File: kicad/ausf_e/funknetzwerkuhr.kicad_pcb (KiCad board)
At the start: 2 copper layers, 100 x 80 mm, 110 parts, among them J1 Jack-DC, J2 Conn_01x04_Male, J3 Conn_01x02_Male, J4 Conn_01x04_Male, Q1 IRF640, Q10 MMBTA42, Q11 MMBTA42, Q12 MMBTA42, Q13 MMBTA42, Q14 MMBTA42, Q15 MMBTA42, Q16 MMBTA42, Q17 MMBTA42, Q18 MMBTA42, Q19 MMBTA42, Q2 MMBTA42, Q20 MMBTA42, Q21 MMBTA42, Q22 MMBTA42, Q3 MMBTA92, Q4 MMBTA42, Q5 MMBTA92, Q6 MMBTA42, Q7 MMBTA92, Q8 MMBTA42, Q9 MMBTA92, T1 IN-12, T2 IN-12, T3 IN-12, T4 IN-12, U1 74HC595, U2 74HC595, U3 74HC595, U4 max1771, U5 NCP1117-33G, U6 ESP-12E

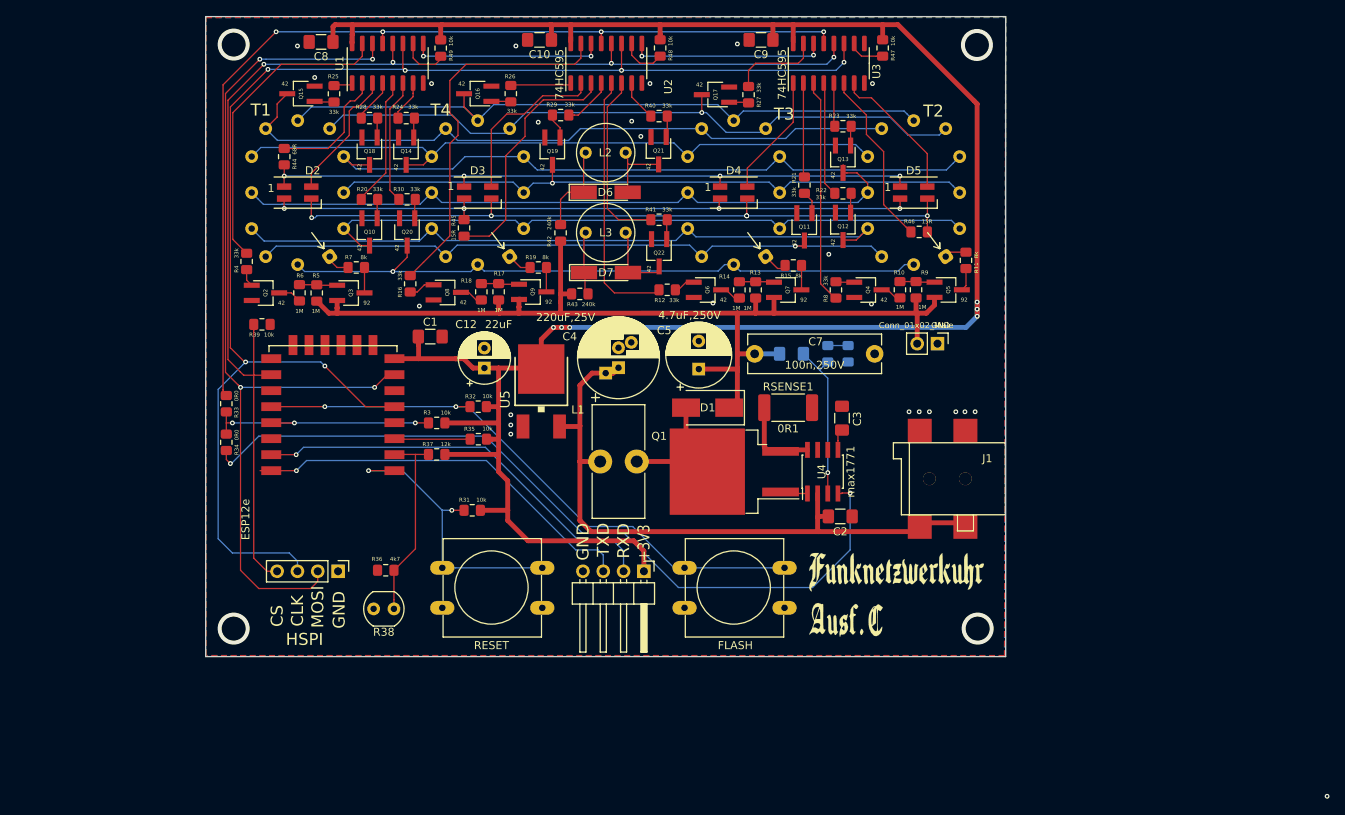
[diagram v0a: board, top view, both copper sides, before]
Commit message: Switched from NTPTime to ezTime
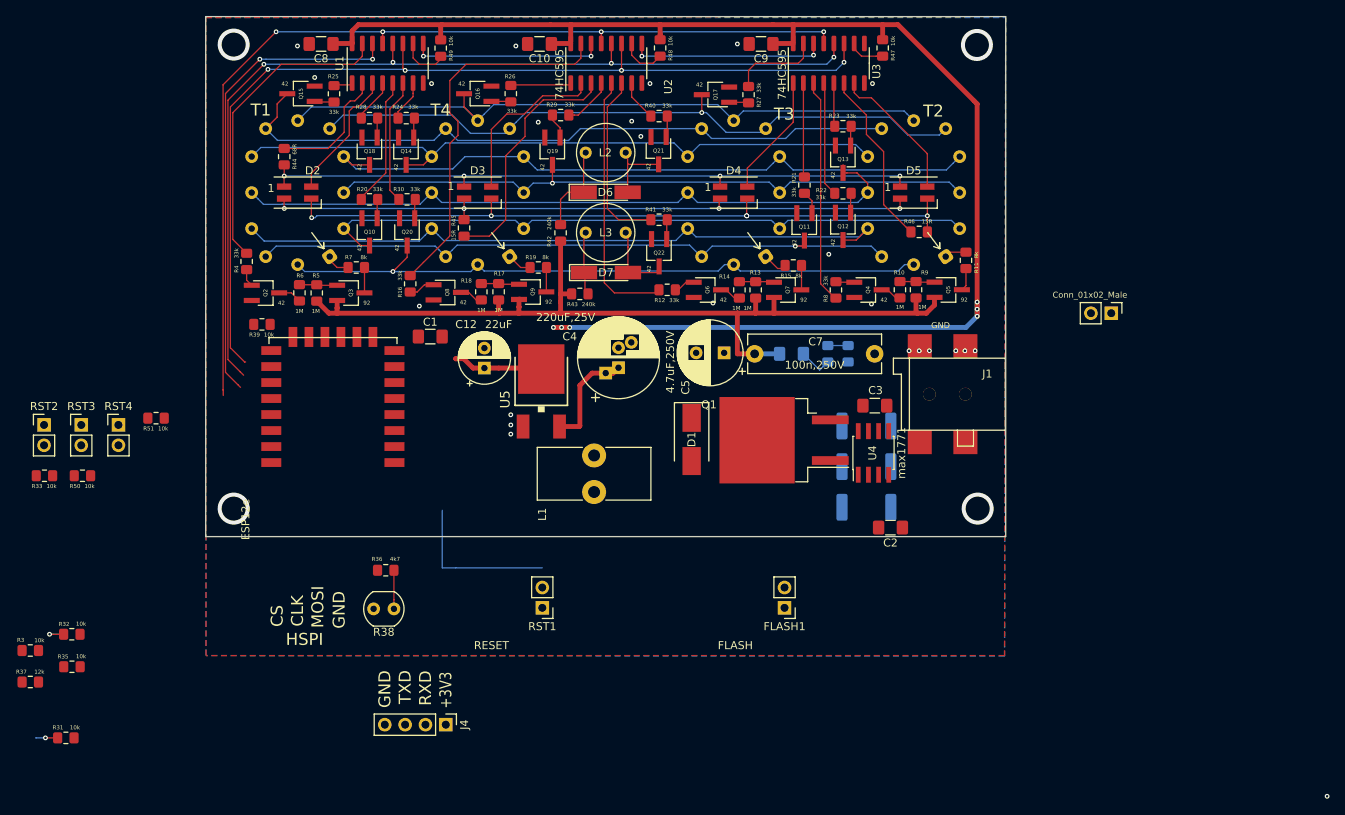
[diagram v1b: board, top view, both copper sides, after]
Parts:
- removed G***: LOGO, PartsStash:Funknetzwerkuhr_Ausf_C
- removed J2: Conn_01x04_Male, Connector_PinHeader_2.54mm:PinHeader_1x04_P2.54mm_Vertical
- removed R34: 0R0, PartsStash:R_0805_2012Metric_Pad1.15x1.40mm_HandSolder_Value
- added R50: 10k, PartsStash:R_0805_2012Metric_Pad1.15x1.40mm_HandSolder_Value, F.Cu at (34.6, 112.4)
- added R51: 10k, PartsStash:R_0805_2012Metric_Pad1.15x1.40mm_HandSolder_Value, F.Cu at (43.8, 105.2)
- added RSENSE2: 0R1, Resistor_SMD:R_2512_6332Metric_Pad1.40x3.35mm_HandSolder, B.Cu at (132.6, 106.2)
- added RSENSE3: 0R1, Resistor_SMD:R_2512_6332Metric_Pad1.40x3.35mm_HandSolder, B.Cu at (132.6, 116.3)
- added RST2: SW_DIP_x01, Connector_PinHeader_2.54mm:PinHeader_1x02_P2.54mm_Vertical, F.Cu at (29.8, 106.0)
- added RST3: SW_DIP_x01, Connector_PinHeader_2.54mm:PinHeader_1x02_P2.54mm_Vertical, F.Cu at (34.4, 106.0)
- added RST4: SW_DIP_x01, Connector_PinHeader_2.54mm:PinHeader_1x02_P2.54mm_Vertical, F.Cu at (39.1, 106.0)
- FLASH1, RST1: footprint Button_Switch_THT:SW_PUSH-12mm -> Connector_PinHeader_2.54mm:PinHeader_1x02_P2.54mm_Vertical
- J4: footprint Connector_PinHeader_2.54mm:PinHeader_1x04_P2.54mm_Horizontal -> Connector_PinHeader_2.54mm:PinHeader_1x04_P2.54mm_Vertical
- R33: value 0R0 -> 10k
- RSENSE1: footprint Resistor_SMD:R_2512_6332Metric_Pad1.52x3.35mm_HandSolder -> Resistor_SMD:R_2512_6332Metric_Pad1.40x3.35mm_HandSolder; moved to B.Cu
- moved R3 58.2 mm to (28.1, 134.2)
- moved R31 58.2 mm to (32.5, 145.2)
- moved R37 58.2 mm to (28.1, 138.2)
- moved R32 58.2 mm to (33.3, 132.2)
- moved R35 58.2 mm to (33.3, 136.3)
- moved J4 31.3 mm to (80.0, 143.5)
- moved R33 24.5 mm to (29.8, 112.4), turned to 0 degrees
- moved J3 22.0 mm to (163.2, 92.1)
- moved RSENSE1 12.2 mm to (132.6, 111.3)
- moved J1 10.6 mm to (145.0, 102.2)
- moved Q1 7.36 mm to (122.3, 108.0)
- moved U4 6.77 mm to (133.5, 109.5)
- moved C2 6.43 mm to (135.6, 118.9)
- moved D1 4.44 mm to (110.7, 107.9), turned to 270 degrees
- moved C3 4.39 mm to (133.6, 103.6), turned to 180 degrees
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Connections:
- R33 pad 1: /~OE -> +3V3
- R33 pad 2: BLANK -> BUTTON_A
- U1 pad 13: /~OE -> BLANK
- U2 pad 13: /~OE -> BLANK
- U3 pad 13: /~OE -> BLANK
- U4 pad 4: Net-(R34-Pad1) -> BLANK
- U6 pad 14: Net-(U6-Pad14) -> BUTTON_A
- U6 pad 4: Net-(U6-Pad4) -> BUTTON_C
- U6 pad 6: Net-(U6-Pad6) -> BUTTON_B
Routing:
- net /~OE: track 120.4 -> 0.00 mm, vias 4 -> 0
- net Net-(R34-Pad1): track 99.8 -> 0.00 mm, vias 2 -> 0
- net BLANK: track 30.3 -> 120.4 mm, vias 3 -> 4
- net +3V3: track 278.0 -> 199.7 mm
- net FLASH: track 73.6 -> 3.28 mm, vias 2 -> 1
- net +9V: track 83.7 -> 13.9 mm
- net HSPI_CLK: track 177.8 -> 121.7 mm, vias 6 -> 4
- net HSPI_MOSI: track 115.7 -> 59.9 mm, vias 4 -> 2
- net /RXD: track 51.9 -> 0.00 mm, vias 1 -> 0
- net /TXD: track 50.4 -> 0.00 mm, vias 1 -> 0
- net HSPI_CS: track 157.8 -> 120.8 mm
- net ADC: track 25.4 -> 4.83 mm
- net Net-(R1-Pad2): track 20.2 -> 4.31 mm, vias 1 -> 0
- net 180V: track 126.9 -> 111.1 mm
- net RESET: track 36.2 -> 22.4 mm, vias 2 -> 1
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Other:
- board size 100 x 80 mm -> 100 x 65 mm
